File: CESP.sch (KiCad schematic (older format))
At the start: 18 parts, among them K1 CONN_3, P1 CONN_7, U1 7555, U2 LM741, U3 7805-REG

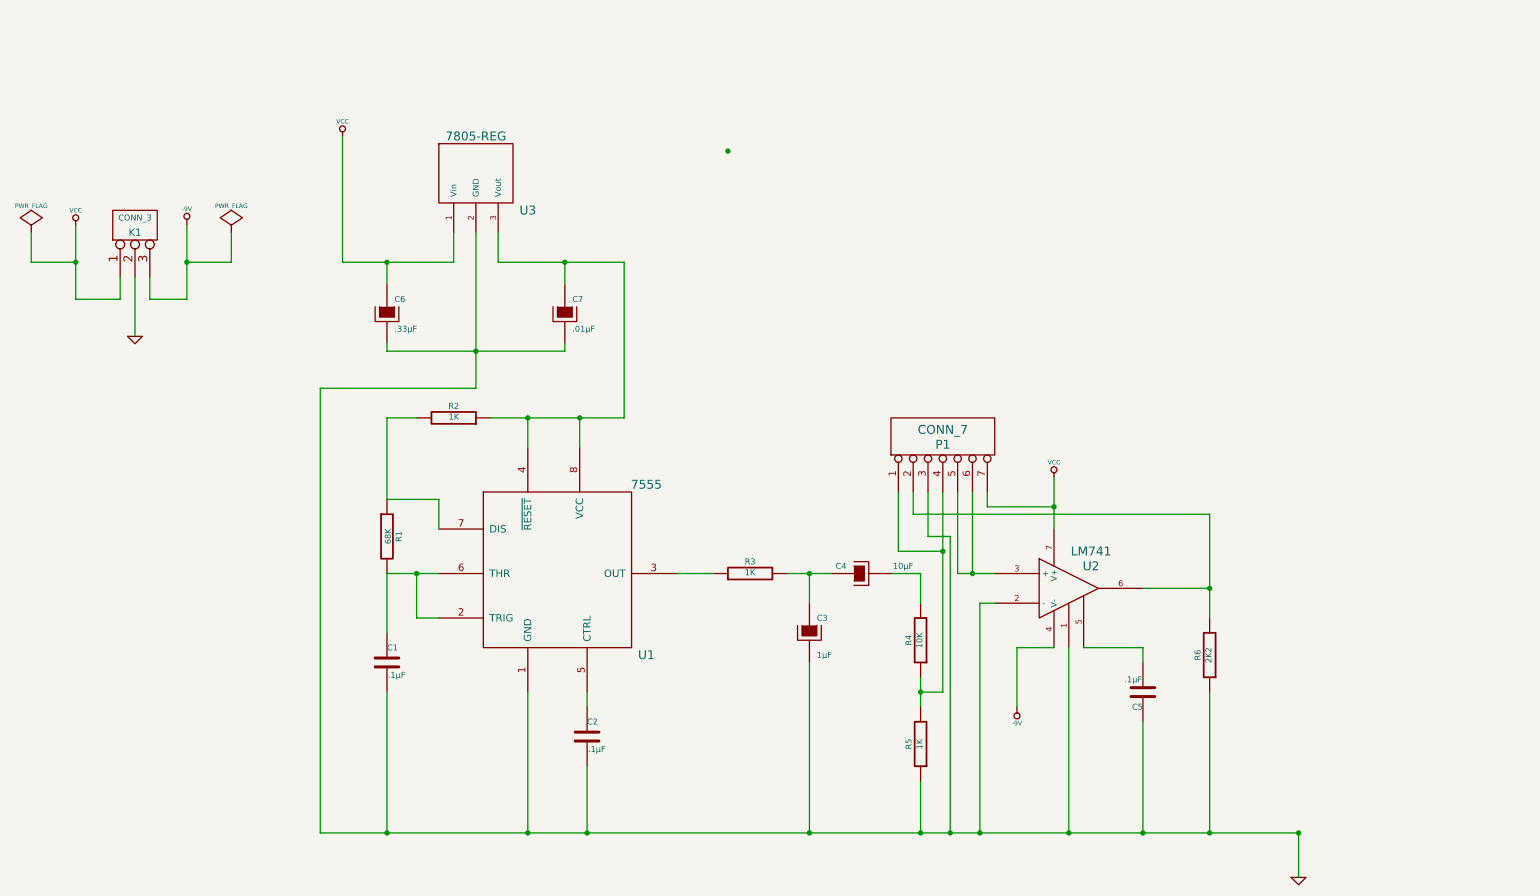
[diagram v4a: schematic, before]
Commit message: Added TSSOP, MSOP and regenerated gerbers...
1. TSSOP 555 blinky circuit added with teeny components to backside
copper.
2. MSOP pads added to back, not connected to anything.
3. Gerbers updated.  Trial run through OshPark for validation
successful.
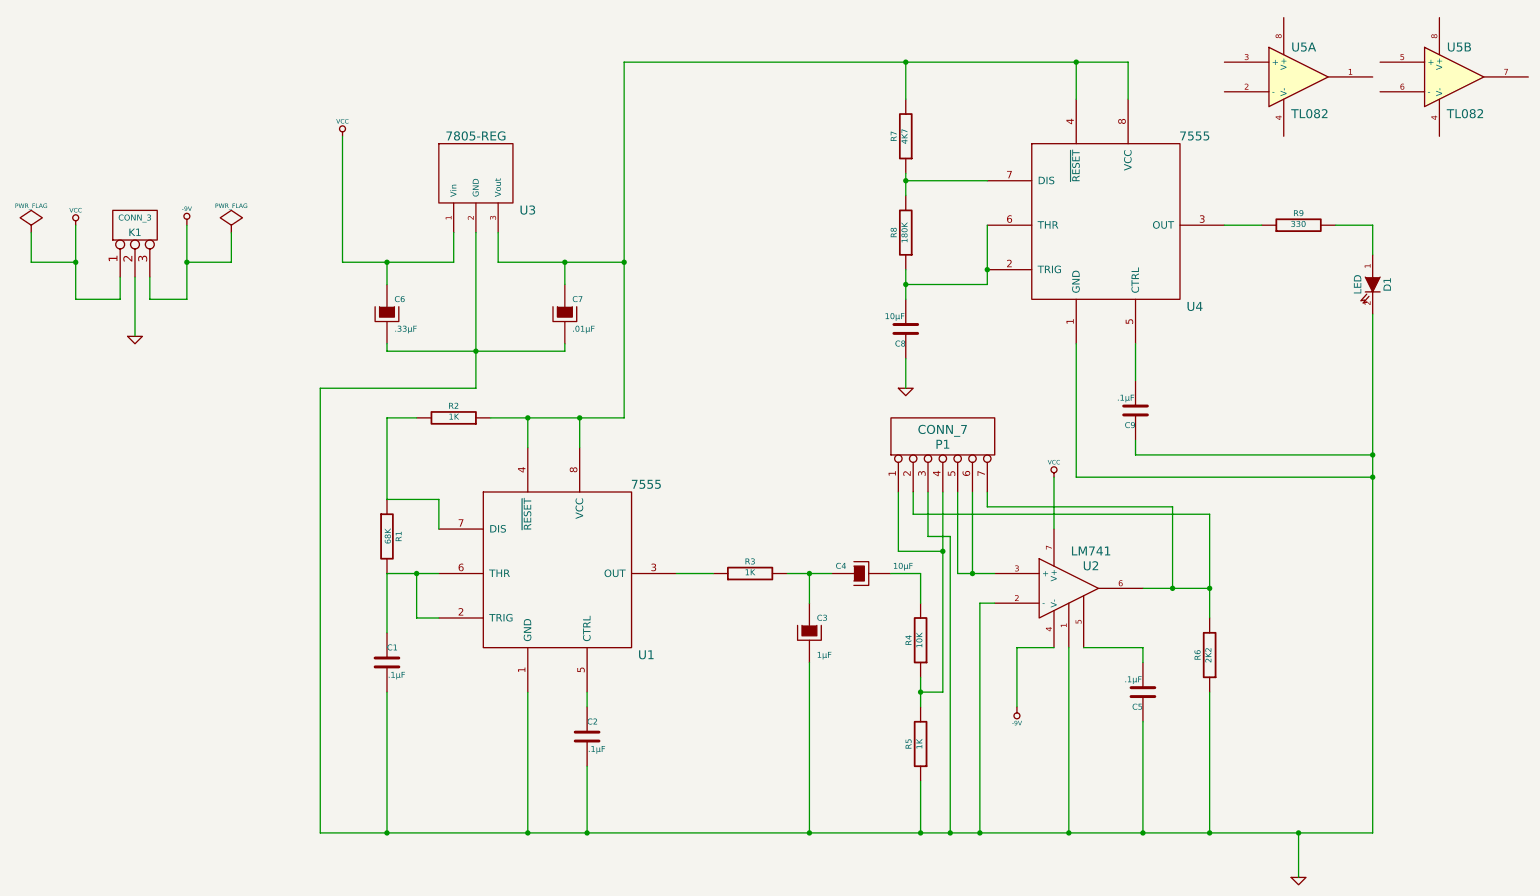
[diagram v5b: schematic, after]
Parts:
- added C8: 10µF, ~, symbol C
- added C9: .1µF, ~, symbol C
- added D1: LED, ~, symbol LED
- added R7: 4K7, ~, symbol R
- added R8: 180K, ~, symbol R
- added R9: 330, ~, symbol R
- added U4: 7555, ~, symbol 7555
- added U5: TL082, symbol TL082
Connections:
- net GND: now also C8.1, C9.1, D1.2 (K), U4.1 (GND)
- net VCC: no longer P1.7 (P7)
- net at C7.1, R2.1, U1.4 (~RESET)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: now also R7.2, U4.4 (~RESET), U4.8 (VCC)
- net at P1.2 (P2), R6.2, U2.6: now also P1.7 (P7)
- new net: C8.2, R8.1, U4.2 (TRIG), U4.6 (THR)
- new net: R9.1, U4.3 (OUT)
- new net: C9.2, U4.5 (CTRL)
- new net: R7.1, R8.2, U4.7 (DIS)
- new net: D1.1 (A), R9.2
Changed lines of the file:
@@
 	3200 4400 3200 4800
 Wire Wire Line
-	3900 3350 4800 3350
+	4800 3350 3900 3350
 Wire Wire Line
 	3400 3350 3200 3350
@@
 	3950 2300 4800 2300
 Wire Wire Line
-	4800 2300 4800 3350
+	4800 950  4800 3350
 Wire Wire Line
 	4400 2900 4400 2850
@@
 	3200 5200 3200 6150
 Wire Wire Line
-	2750 6150 9350 6150
+	2750 6150 9850 6150
 Wire Wire Line
 	4150 5200 4150 6150
@@
 Connection ~ 3200 6150
 Connection ~ 9350 6150
-Connection ~ 5500 1550
 Wire Wire Line
 	7300 4600 7200 4600
@@
 $EndComp
 $Comp
-L GND #PWR7
+L GND #PWR8
 U 1 1 52E6AE37
 P 9350 6450
-F 0 "#PWR7" H 9350 6450 30  0001 C CNN
+F 0 "#PWR8" H 9350 6450 30  0001 C CNN
 F 1 "GND" H 9350 6380 30  0001 C CNN
 F 2 "" H 9350 6450 60  0000 C CNN
@@
 $EndComp
 $Comp
-L VCC #PWR6
+L VCC #PWR7
 U 1 1 52E6AE98
 P 7700 3750
-F 0 "#PWR6" H 7700 3850 30  0001 C CNN
+F 0 "#PWR7" H 7700 3850 30  0001 C CNN
 F 1 "VCC" H 7700 3850 30  0000 C CNN
 F 2 "" H 7700 3750 60  0000 C CNN
@@
 $EndComp
 $Comp
-L -9V #PWR5
+L -9V #PWR6
 U 1 1 52E6AF0B
 P 7450 5300
-F 0 "#PWR5" H 7450 5270 20  0001 C CNN
+F 0 "#PWR6" H 7450 5270 20  0001 C CNN
 F 1 "-9V" H 7450 5410 30  0000 C CNN
 F 2 "~" H 7450 5300 60  0000 C CNN
@@
 Connection ~ 1100 2300
 Wire Wire Line
-	7700 4100 7700 3750
-Connection ~ 7700 3950
-Wire Wire Line
 	7200 4600 7200 6150
 Wire Wire Line
@@
 	7050 4400 7300 4400
 Connection ~ 7150 4400
-Wire Wire Line
-	7250 3950 7700 3950
 $Comp
 L CONN_7 P1
@@
 	7000 4150 7000 6150
 Connection ~ 7000 6150
+Wire Wire Line
+	7700 3750 7700 4100
+Wire Wire Line
+	7250 3950 8500 3950
+Wire Wire Line
+	8500 3950 8500 4500
+Connection ~ 8500 4500
+$Comp
+L 7555 U4
+U 1 1 52E7FB88
+P 8050 2050
+F 0 "U4" H 8650 1500 60  0000 C CNN
+F 1 "7555" H 8650 2650 60  0000 C CNN
+F 2 "~" H 8100 1700 60  0000 C CNN
+F 3 "~" H 8100 1700 60  0000 C CNN
+	1    8050 2050
+	1    0    0    -1
+$EndComp
+$Comp
+L R R9
+U 1 1 52E7FBA5
+P 9350 2050
+F 0 "R9" V 9430 2050 40  0000 C CNN
+F 1 "330" V 9357 2051 40  0000 C CNN
+F 2 "~" V 9280 2050 30  0000 C CNN
+F 3 "~" H 9350 2050 30  0000 C CNN
+	1    9350 2050
+	0    -1   -1   0
+$EndComp
+$Comp
+L LED D1
+U 1 1 52E7FBB4
+P 9850 2450
+F 0 "D1" H 9850 2550 50  0000 C CNN
+F 1 "LED" H 9850 2350 50  0000 C CNN
+F 2 "~" H 9850 2450 60  0000 C CNN
+F 3 "~" H 9850 2450 60  0000 C CNN
+	1    9850 2450
+	0    1    1    0
+$EndComp
+$Comp
+L C C9
+U 1 1 52E7FBC1
+P 8250 3300
+F 0 "C9" H 8250 3400 40  0000 L CNN
+F 1 ".1µF" H 8256 3215 40  0000 L CNN
+F 2 "~" H 8288 3150 30  0000 C CNN
+F 3 "~" H 8250 3300 60  0000 C CNN
+	1    8250 3300
+	-1   0    0    1
+$EndComp
+$Comp
+L R R7
+U 1 1 52E7FBCC
+P 6700 1450
+F 0 "R7" V 6780 1450 40  0000 C CNN
+F 1 "4K7" V 6707 1451 40  0000 C CNN
+F 2 "~" V 6630 1450 30  0000 C CNN
+F 3 "~" H 6700 1450 30  0000 C CNN
+	1    6700 1450
+	-1   0    0    1
+$EndComp
+$Comp
+L R R8
+U 1 1 52E7FBE8
+P 6700 2100
+F 0 "R8" V 6780 2100 40  0000 C CNN
+F 1 "180K" V 6707 2101 40  0000 C CNN
+F 2 "~" V 6630 2100 30  0000 C CNN
+F 3 "~" H 6700 2100 30  0000 C CNN
+	1    6700 2100
+	-1   0    0    1
+$EndComp
+$Comp
+L C C8
+U 1 1 52E7FBEE
+P 6700 2750
+F 0 "C8" H 6700 2850 40  0000 L CNN
+F 1 "10µF" H 6706 2665 40  0000 L CNN
+F 2 "~" H 6738 2600 30  0000 C CNN
+F 3 "~" H 6700 2750 60  0000 C CNN
+	1    6700 2750
+	-1   0    0    1
+$EndComp
+Wire Wire Line
+	4800 950  8200 950
+Wire Wire Line
+	8200 950  8200 1200
+Connection ~ 4800 2300
+Wire Wire Line
+	7850 1200 7850 950
+Connection ~ 7850 950
+Wire Wire Line
+	6700 1200 6700 950
+Connection ~ 6700 950
+Wire Wire Line
+	6700 1700 6700 1850
+Wire Wire Line
+	6700 2350 6700 2550
+Wire Wire Line
+	7250 1750 6700 1750
+Connection ~ 6700 1750
+Wire Wire Line
+	7250 2050 7250 2450
+Wire Wire Line
+	7250 2450 6700 2450
+Connection ~ 6700 2450
+Connection ~ 7250 2350
+$Comp
+L GND #PWR5
+U 1 1 52E7FF6A
+P 6700 3150
+F 0 "#PWR5" H 6700 3150 30  0001 C CNN
+F 1 "GND" H 6700 3080 30  0001 C CNN
+F 2 "" H 6700 3150 60  0000 C CNN
+F 3 "" H 6700 3150 60  0000 C CNN
+	1    6700 3150
+	1    0    0    -1
+$EndComp
+Wire Wire Line
+	6700 3150 6700 2950
+Wire Wire Line
+	8850 2050 9100 2050
+Wire Wire Line
+	9600 2050 9850 2050
+Wire Wire Line
+	9850 2050 9850 2250
+Wire Wire Line
+	9850 6150 9850 2650
+Wire Wire Line
+	8250 2850 8250 3100
+Wire Wire Line
+	8250 3500 8250 3600
+Wire Wire Line
+	8250 3600 9850 3600
+Connection ~ 9850 3600
+Wire Wire Line
+	7850 2850 7850 3750
+Wire Wire Line
+	7850 3750 9850 3750
+Connection ~ 9850 3750
+$Comp
+L TL082 U5
+U 1 1 52E80542
+P 9350 1050
+F 0 "U5" H 9300 1250 60  0000 L CNN
+F 1 "TL082" H 9300 800 60  0000 L CNN
+F 2 "" H 9350 1050 60  0000 C CNN
+F 3 "" H 9350 1050 60  0000 C CNN
+	1    9350 1050
+	1    0    0    -1
+$EndComp
+$Comp
+L TL082 U5
+U 2 1 52E8054F
+P 10400 1050
+F 0 "U5" H 10350 1250 60  0000 L CNN
+F 1 "TL082" H 10350 800 60  0000 L CNN
+F 2 "" H 10400 1050 60  0000 C CNN
+F 3 "" H 10400 1050 60  0000 C CNN
+	2    10400 1050
+	1    0    0    -1
+$EndComp
 $EndSCHEMATC
